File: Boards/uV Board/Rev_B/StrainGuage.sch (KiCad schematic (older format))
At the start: 0 parts

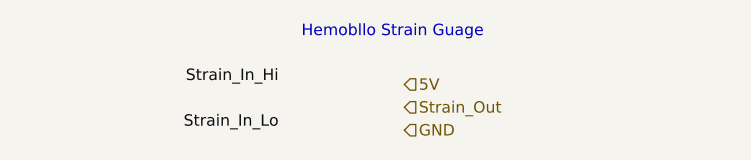
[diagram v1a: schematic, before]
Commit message: Added regulator to ADC and micro boards. Added actual connectors for the strain gauge modules.
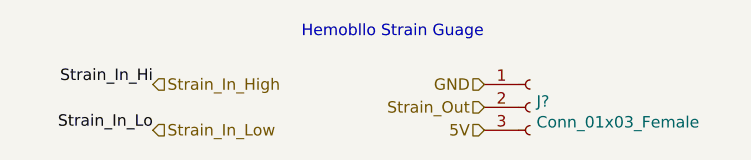
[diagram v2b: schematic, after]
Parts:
- added J?: Conn_01x03_Female, symbol Connector:Conn_01x03_Female
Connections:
- net 5V: now also J?.3 (Pin_3)
- net GND: now also J?.1 (Pin_1)
- net Strain_Out: now also J?.2 (Pin_2)
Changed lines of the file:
@@
 $Descr A4 11693 8268
 encoding utf-8
-Sheet 6 6
+Sheet 4 7
 Title ""
 Date ""
@@
 Text Notes 2450 1150 0    50   ~ 0
 Hemobllo Strain Guage
-Text HLabel 2900 1350 2    50   Input ~ 0
+Text HLabel 3250 1550 0    50   Input ~ 0
 5V
-Text HLabel 2900 1550 2    50   Input ~ 0
+Text HLabel 3250 1350 0    50   Input ~ 0
 GND
-Text HLabel 2900 1450 2    50   Input ~ 0
+Text HLabel 3250 1450 0    50   Input ~ 0
 Strain_Out
-Text Label 2350 1350 2    50   ~ 0
+Text Label 1800 1350 2    50   ~ 0
 Strain_In_Hi
-Text Label 2350 1550 2    50   ~ 0
+Text Label 1800 1550 2    50   ~ 0
 Strain_In_Lo
+$Comp
+L Connector:Conn_01x03_Female J?
+U 1 1 61602119
+P 3450 1450
+AR Path="/614FDE40/61602119" Ref="J?"  Part="1"
+AR Path="/6153C564/61602119" Ref="J?"  Part="1"
+AR Path="/61575905/61602119" Ref="J?"  Part="1"
+AR Path="/61575900/61602119" Ref="J?"  Part="1"
+F 0 "J?" H 3478 1476 50  0000 L CNN
+F 1 "Conn_01x03_Female" H 3478 1385 50  0000 L CNN
+F 2 "" H 3450 1450 50  0001 C CNN
+F 3 "~" H 3450 1450 50  0001 C CNN
+	1    3450 1450
+	1    0    0    -1
+$EndComp
+Text HLabel 1800 1350 2    50   Input ~ 0
+Strain_In_High
+Text HLabel 1800 1550 2    50   Input ~ 0
+Strain_In_Low
 $EndSCHEMATC

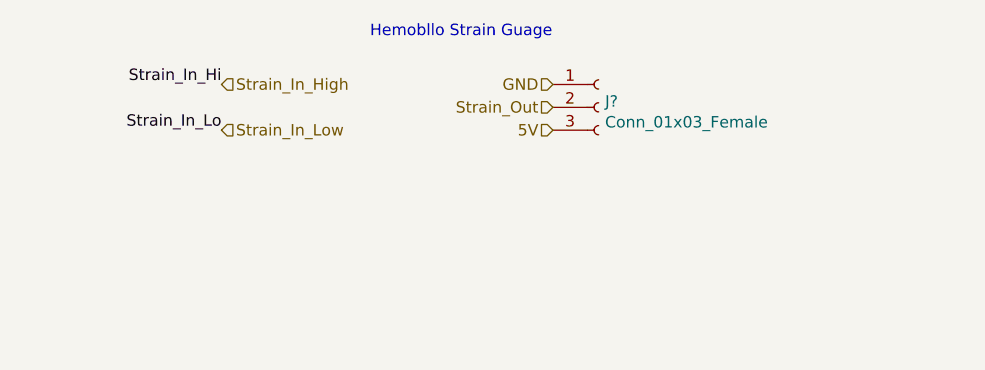
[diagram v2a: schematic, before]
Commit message: Fixed regulator nonsense on ADC board. Rules checked both ADC and micro boards. Fixed interconnect on ADC board.
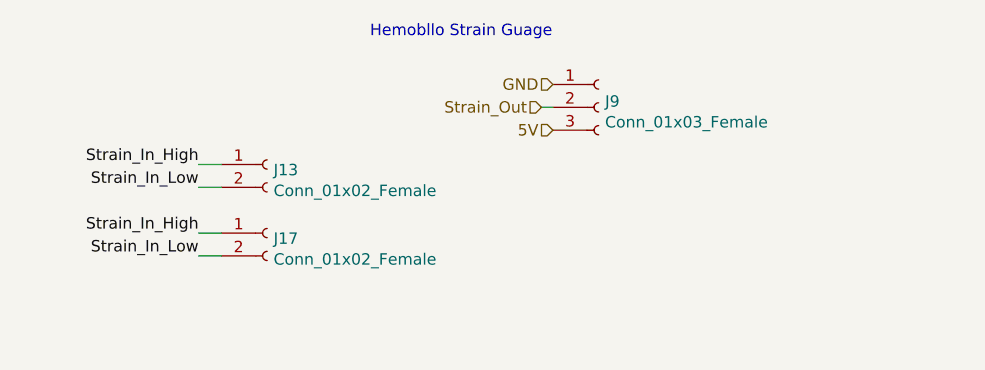
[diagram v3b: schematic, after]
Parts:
- added J10, J14: Conn_01x02_Female, symbol Connector:Conn_01x02_Female
- gave numbers to parts that had none: 1
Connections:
- net Strain_In_High: now also J10.1 (Pin_1), J14.1 (Pin_1)
- net Strain_In_Low: now also J10.2 (Pin_2), J14.2 (Pin_2)
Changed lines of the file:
@@
 $Descr A4 11693 8268
 encoding utf-8
-Sheet 4 7
+Sheet 6 7
 Title ""
 Date ""
@@
 Text HLabel 3250 1350 0    50   Input ~ 0
 GND
-Text HLabel 3250 1450 0    50   Input ~ 0
+Text HLabel 3200 1450 0    50   Input ~ 0
 Strain_Out
-Text Label 1800 1350 2    50   ~ 0
-Strain_In_Hi
-Text Label 1800 1550 2    50   ~ 0
-Strain_In_Lo
 $Comp
-L Connector:Conn_01x03_Female J?
+L Connector:Conn_01x03_Female J9
 U 1 1 61602119
 P 3450 1450
-AR Path="/614FDE40/61602119" Ref="J?"  Part="1"
-AR Path="/6153C564/61602119" Ref="J?"  Part="1"
-AR Path="/61575905/61602119" Ref="J?"  Part="1"
-AR Path="/61575900/61602119" Ref="J?"  Part="1"
-F 0 "J?" H 3478 1476 50  0000 L CNN
+AR Path="/614FDE40/61602119" Ref="J9"  Part="1"
+AR Path="/6153C564/61602119" Ref="J6"  Part="1"
+AR Path="/61575905/61602119" Ref="J8"  Part="1"
+AR Path="/61575900/61602119" Ref="J7"  Part="1"
+F 0 "J9" H 3478 1476 50  0000 L CNN
 F 1 "Conn_01x03_Female" H 3478 1385 50  0000 L CNN
 F 2 "" H 3450 1450 50  0001 C CNN
@@
 	1    0    0    -1
 $EndComp
-Text HLabel 1800 1350 2    50   Input ~ 0
+Wire Wire Line
+	3200 1450 3250 1450
+$Comp
+L Connector:Conn_01x02_Female J10
+U 1 1 615FC90F
+P 2000 1700
+AR Path="/6153C564/615FC90F" Ref="J10"  Part="1"
+AR Path="/61575900/615FC90F" Ref="J11"  Part="1"
+AR Path="/61575905/615FC90F" Ref="J12"  Part="1"
+AR Path="/614FDE40/615FC90F" Ref="J13"  Part="1"
+F 0 "J13" H 2028 1676 50  0000 L CNN
+F 1 "Conn_01x02_Female" H 2028 1585 50  0000 L CNN
+F 2 "" H 2000 1700 50  0001 C CNN
+F 3 "~" H 2000 1700 50  0001 C CNN
+	1    2000 1700
+	1    0    0    -1
+$EndComp
+Wire Wire Line
+	1700 1700 1800 1700
+Wire Wire Line
+	1800 1800 1700 1800
+Text Label 1700 1700 2    50   ~ 0
 Strain_In_High
-Text HLabel 1800 1550 2    50   Input ~ 0
+Text Label 1700 1800 2    50   ~ 0
+Strain_In_Low
+$Comp
+L Connector:Conn_01x02_Female J14
+U 1 1 61600C0D
+P 2000 2000
+AR Path="/6153C564/61600C0D" Ref="J14"  Part="1"
+AR Path="/61575900/61600C0D" Ref="J15"  Part="1"
+AR Path="/61575905/61600C0D" Ref="J16"  Part="1"
+AR Path="/614FDE40/61600C0D" Ref="J17"  Part="1"
+F 0 "J17" H 2028 1976 50  0000 L CNN
+F 1 "Conn_01x02_Female" H 2028 1885 50  0000 L CNN
+F 2 "" H 2000 2000 50  0001 C CNN
+F 3 "~" H 2000 2000 50  0001 C CNN
+	1    2000 2000
+	1    0    0    -1
+$EndComp
+Wire Wire Line
+	1700 2000 1800 2000
+Wire Wire Line
+	1800 2100 1700 2100
+Text Label 1700 2000 2    50   ~ 0
+Strain_In_High
+Text Label 1700 2100 2    50   ~ 0
 Strain_In_Low
 $EndSCHEMATC

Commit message: Moved around components on the ADC board PCB. Assigned footprints to microVolt board components.
Tried to add 6-pin spring connector to custom schematics list.
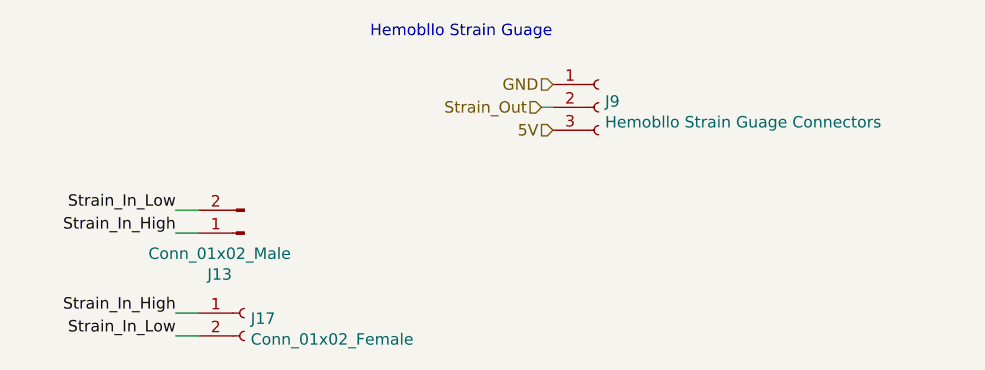
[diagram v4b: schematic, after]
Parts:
- removed J10: Conn_01x02_Female, symbol Connector:Conn_01x02_Female
- added J13: Conn_01x02_Male, Connector_PinHeader_2.54mm:PinHeader_1x02_P2.54mm_Vertical, symbol Connector:Conn_01x02_Male
- J14: footprint (none) -> Connector_PinSocket_2.54mm:PinSocket_1x02_P2.54mm_Vertical
- J9: value Conn_01x03_Female -> Hemobllo Strain Guage Connectors; footprint (none) -> Connector_PinSocket_2.54mm:PinSocket_1x03_P2.54mm_Vertical
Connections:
- net Strain_In_High: now also J13.1 (Pin_1)
- net Strain_In_Low: now also J13.2 (Pin_2)
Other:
- moved on the sheet: J17
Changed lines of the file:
@@
 AR Path="/61575900/61602119" Ref="J7"  Part="1"
 F 0 "J9" H 3478 1476 50  0000 L CNN
-F 1 "Conn_01x03_Female" H 3478 1385 50  0000 L CNN
-F 2 "" H 3450 1450 50  0001 C CNN
+F 1 "Hemobllo Strain Guage Connectors" H 3478 1385 50  0000 L CNN
+F 2 "Connector_PinSocket_2.54mm:PinSocket_1x03_P2.54mm_Vertical" H 3450 1450 50  0001 C CNN
 F 3 "~" H 3450 1450 50  0001 C CNN
 	1    3450 1450
@@
 Wire Wire Line
 	3200 1450 3250 1450
-$Comp
-L Connector:Conn_01x02_Female J10
-U 1 1 615FC90F
-P 2000 1700
-AR Path="/6153C564/615FC90F" Ref="J10"  Part="1"
-AR Path="/61575900/615FC90F" Ref="J11"  Part="1"
-AR Path="/61575905/615FC90F" Ref="J12"  Part="1"
-AR Path="/614FDE40/615FC90F" Ref="J13"  Part="1"
-F 0 "J13" H 2028 1676 50  0000 L CNN
-F 1 "Conn_01x02_Female" H 2028 1585 50  0000 L CNN
-F 2 "" H 2000 1700 50  0001 C CNN
-F 3 "~" H 2000 1700 50  0001 C CNN
-	1    2000 1700
-	1    0    0    -1
-$EndComp
 Wire Wire Line
-	1700 1700 1800 1700
+	1600 1900 1700 1900
 Wire Wire Line
-	1800 1800 1700 1800
-Text Label 1700 1700 2    50   ~ 0
+	1700 2000 1600 2000
+Text Label 1600 2000 2    50   ~ 0
 Strain_In_High
-Text Label 1700 1800 2    50   ~ 0
+Text Label 1600 1900 2    50   ~ 0
 Strain_In_Low
 $Comp
 L Connector:Conn_01x02_Female J14
 U 1 1 61600C0D
-P 2000 2000
+P 1900 2350
 AR Path="/6153C564/61600C0D" Ref="J14"  Part="1"
 AR Path="/61575900/61600C0D" Ref="J15"  Part="1"
 AR Path="/61575905/61600C0D" Ref="J16"  Part="1"
 AR Path="/614FDE40/61600C0D" Ref="J17"  Part="1"
-F 0 "J17" H 2028 1976 50  0000 L CNN
-F 1 "Conn_01x02_Female" H 2028 1885 50  0000 L CNN
-F 2 "" H 2000 2000 50  0001 C CNN
-F 3 "~" H 2000 2000 50  0001 C CNN
-	1    2000 2000
+F 0 "J17" H 1928 2326 50  0000 L CNN
+F 1 "Conn_01x02_Female" H 1928 2235 50  0000 L CNN
+F 2 "Connector_PinSocket_2.54mm:PinSocket_1x02_P2.54mm_Vertical" H 1900 2350 50  0001 C CNN
+F 3 "~" H 1900 2350 50  0001 C CNN
+	1    1900 2350
 	1    0    0    -1
 $EndComp
 Wire Wire Line
-	1700 2000 1800 2000
+	1600 2350 1700 2350
 Wire Wire Line
-	1800 2100 1700 2100
-Text Label 1700 2000 2    50   ~ 0
+	1700 2450 1600 2450
+Text Label 1600 2350 2    50   ~ 0
 Strain_In_High
-Text Label 1700 2100 2    50   ~ 0
+Text Label 1600 2450 2    50   ~ 0
 Strain_In_Low
+$Comp
+L Connector:Conn_01x02_Male J13
+U 1 1 61ECA2C8
+P 1900 2000
+AR Path="/614FDE40/61ECA2C8" Ref="J13"  Part="1"
+AR Path="/6153C564/61ECA2C8" Ref="J10"  Part="1"
+AR Path="/61575900/61ECA2C8" Ref="J11"  Part="1"
+AR Path="/61575905/61ECA2C8" Ref="J12"  Part="1"
+F 0 "J13" H 2008 2181 50  0000 C CNN
+F 1 "Conn_01x02_Male" H 2008 2090 50  0000 C CNN
+F 2 "Connector_PinHeader_2.54mm:PinHeader_1x02_P2.54mm_Vertical" H 1900 2000 50  0001 C CNN
+F 3 "~" H 1900 2000 50  0001 C CNN
+	1    1900 2000
+	-1   0    0    1
+$EndComp
 $EndSCHEMATC
